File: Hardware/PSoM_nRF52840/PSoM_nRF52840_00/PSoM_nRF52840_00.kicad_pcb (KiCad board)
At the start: 6 copper layers, 26.3 x 23.2 mm, 52 parts, among them J1 Bare PCB USB C, J101 DF40C-60DP-0.4V(51), J401 Conn_01x01_Pin, J402 Conn_01x01_Pin, SW461 SW_Push, U201 NPM1300-QEAA-R, U401 nRF52840-QIAA-aQFN73, Y401 830108161301

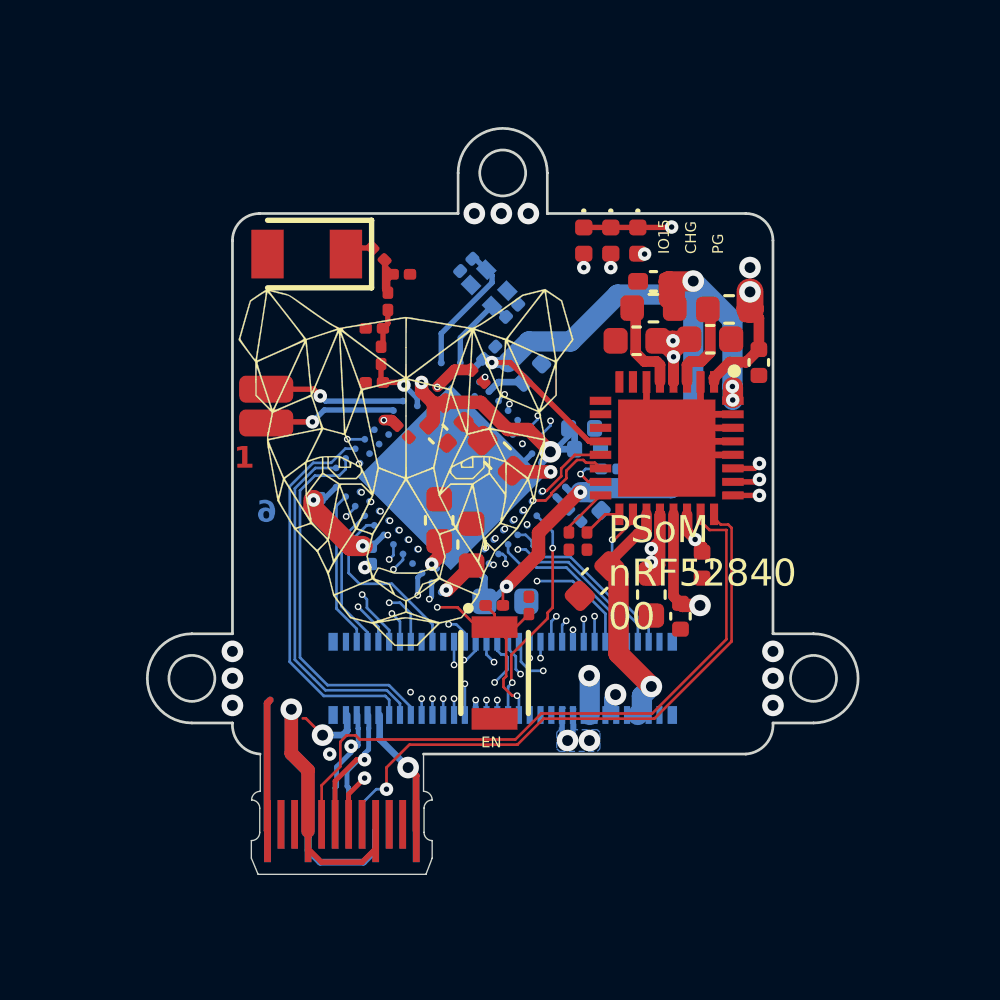
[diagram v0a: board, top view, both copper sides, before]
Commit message: rf routing to do
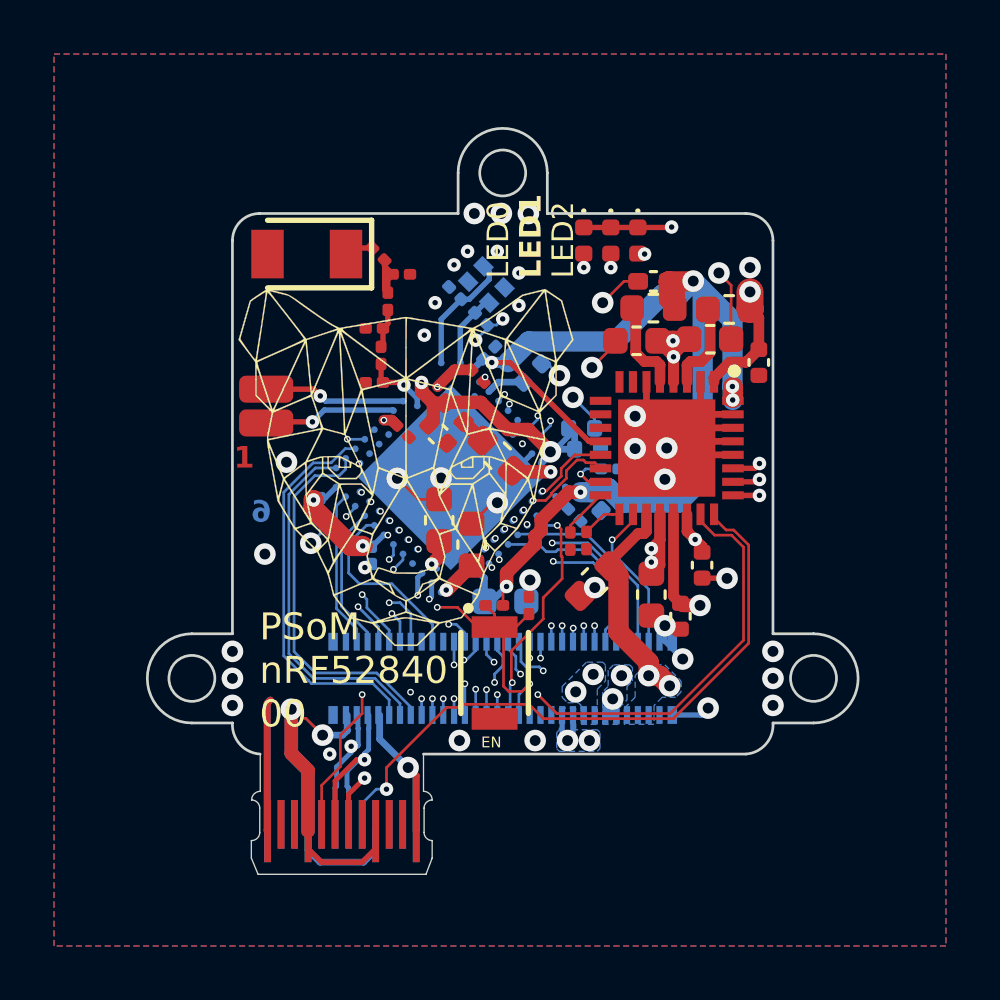
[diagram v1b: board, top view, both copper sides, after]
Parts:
- moved C402 1.19 mm to (135.2, 92.9), turned to -45 degrees
- moved C401 1.12 mm to (134.2, 91.9), turned to 135 degrees
- moved Y401 0.16 mm to (135.4, 91.6)
- moved R204 0.05 mm to (138.5, 101.1)
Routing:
- net GND: track 38.2 -> 64.4 mm, vias 12 -> 44
- net /100_Connectors/CC1: track 24.7 -> 27.0 mm, vias 0 -> 2
- net /200_1S_Charger/3V3_nRF: track 58.9 -> 60.3 mm
- net /100_Connectors/CC2: track 25.5 -> 26.9 mm
- net P11: track 6.37 -> 7.40 mm
- net /100_Connectors/RST: track 17.2 -> 18.2 mm
- net /200_1S_Charger/VBUS_OUT: track 13.5 -> 14.5 mm
- net /100_Connectors/VBAT: track 8.98 -> 8.21 mm, vias 1 -> 2
- net P5: track 6.57 -> 7.32 mm
- net VBUS: track 42.4 -> 43.1 mm, vias 3 -> 4
- net P9: track 6.19 -> 6.92 mm
- net P31: track 17.6 -> 16.9 mm
- net P7: track 6.94 -> 7.62 mm
- net P21: track 5.86 -> 5.19 mm
- net /100_Connectors/VSYS: track 35.6 -> 35.0 mm, vias 6 -> 7
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- added copper zone on B.Cu, net /100_Connectors/VBAT
- added copper zone on B.Cu, net /100_Connectors/VSYS
- added copper zone on B.Cu, net GND
- added copper zone on F.Cu, net GND
- added copper zone on In2.Cu, net GND
- added copper zone on In3.Cu, net GND
- added copper zone on B.Cu, net VBUS
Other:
- board text added: "LED0"
- board text added: "LED1"
- board text added: "LED2"
- board text removed: "CHG"
- board text removed: "IO15"
- board text removed: "PG"

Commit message: still need to do rf
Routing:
- net /400-nRF52840/DEC4_6: track 11.5 -> 12.5 mm
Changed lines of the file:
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@@
 	)
 	(via
-		(at 133.1 93.5)
+		(at 133.1 93.3)
 		(size 0.5)
 		(drill 0.2)
@@
 	)
 	(segment
-		(start 132.998492 95.580295)
-		(end 133.435839 96.017642)
+		(start 133.867642 96.017642)
+		(end 133.898412 95.986872)
 		(width 0.5)
 		(layer "F.Cu")
@@
 	)
 	(segment
-		(start 133.867642 96.017642)
-		(end 133.898412 95.986872)
+		(start 133.435839 96.017642)
+		(end 133.867642 96.017642)
 		(width 0.5)
 		(layer "F.Cu")
@@
 	)
 	(segment
-		(start 133.435839 96.017642)
-		(end 133.867642 96.017642)
+		(start 133.2 94.815)
+		(end 133.049033 94.965967)
 		(width 0.5)
 		(layer "F.Cu")
@@
 	)
 	(segment
-		(start 132.998492 95.251508)
-		(end 132.998492 95.580295)
+		(start 136.94589 96.992767)
+		(end 137.765169 97.812046)
 		(width 0.5)
 		(layer "F.Cu")
@@
 	)
 	(segment
-		(start 136.94589 96.992767)
-		(end 137.765169 97.812046)
+		(start 133.049033 94.965967)
+		(end 133.049033 95.630836)
 		(width 0.5)
 		(layer "F.Cu")
@@
 		(net 75)
 	)
+	(segment
+		(start 133.049033 95.630836)
+		(end 133.435839 96.017642)
+		(width 0.5)
+		(layer "F.Cu")
+		(net 75)
+	)
 	(via
 		(at 137.765169 97.816847)
@@
 	)
 	(via
-		(at 132.998492 95.251508)
+		(at 133.2 94.815)
 		(size 0.5)
 		(drill 0.2)
@@
 	)
 	(segment
+		(start 133.017767 95.232968)
+		(end 133.017767 94.997233)
+		(width 0.5)
+		(layer "B.Cu")
+		(net 75)
+	)
+	(segment
 		(start 137.954621 97.72)
 		(end 137.437184 98.237437)
@@
 	)
 	(segment
+		(start 133.017767 94.997233)
+		(end 133.2 94.815)
+		(width 0.5)
+		(layer "B.Cu")
+		(net 75)
+	)
+	(segment
 		(start 134.43198 94.525861)
 		(end 134.43198 93.215472)
@@
 	)
 	(segment
-		(start 129 97.680761)
-		(end 132.280761 94.4)
+		(start 132.580761 94.1)
+		(end 134.403837 94.1)
 		(width 0.75)
 		(layer "In3.Cu")
@@
 	)
 	(segment
-		(start 129 99.6)
-		(end 129 97.680761)
+		(start 134.703837 94.4)
+		(end 135.595882 94.4)
+		(width 0.75)
+		(layer "In3.Cu")
+		(net 92)
+	)
+	(segment
+		(start 134.403837 94.1)
+		(end 134.703837 94.4)
+		(width 0.75)
+		(layer "In3.Cu")
+		(net 92)
+	)
+	(segment
+		(start 129 97.680761)
+		(end 132.580761 94.1)
 		(width 0.75)
 		(layer "In3.Cu")
@@
 	)
 	(segment
-		(start 132.280761 94.4)
-		(end 135.595882 94.4)
+		(start 129 99.6)
+		(end 129 97.680761)
 		(width 0.75)
 		(layer "In3.Cu")

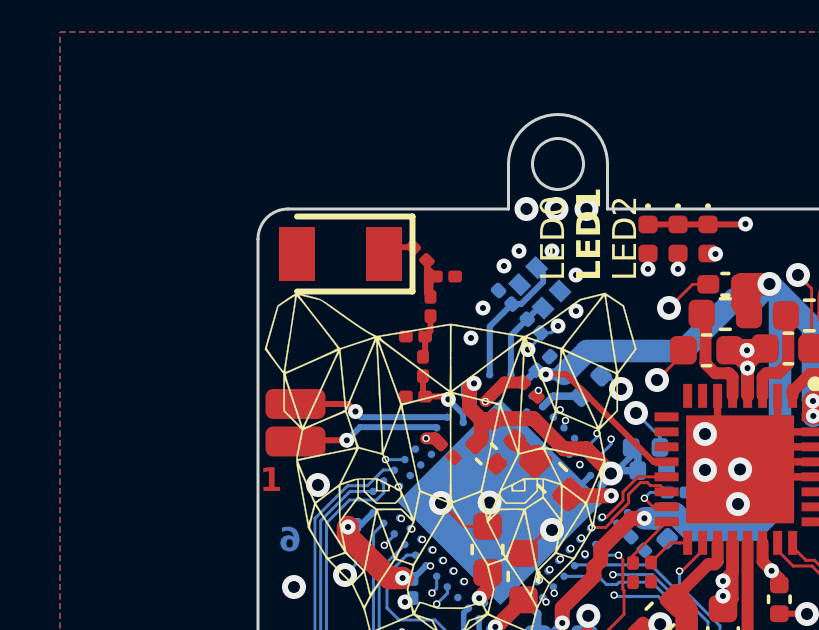
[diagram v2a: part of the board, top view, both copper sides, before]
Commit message: opened ground plane for antenna
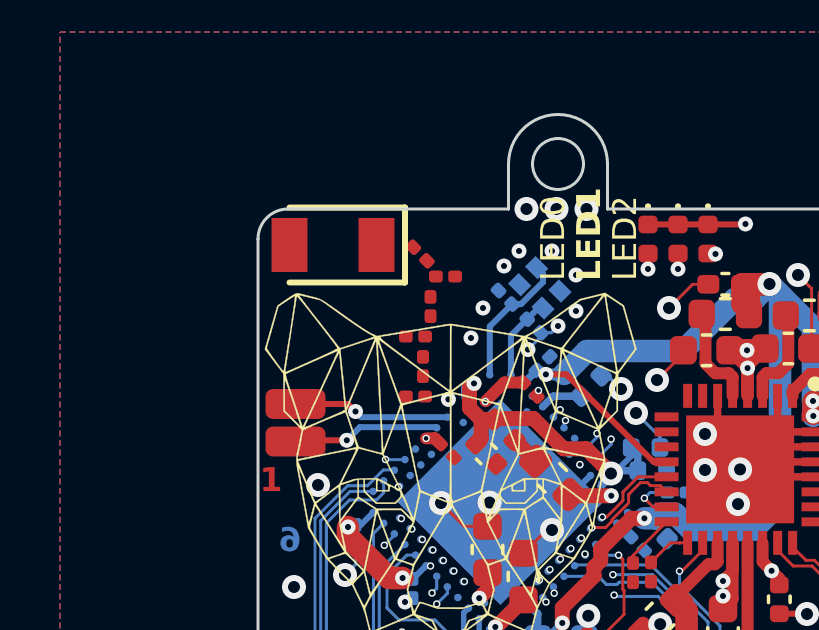
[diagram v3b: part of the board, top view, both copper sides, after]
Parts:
- moved ANT450 0.39 mm to (128.5, 90.2)
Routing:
- net /400-nRF52840/ANT_MATCH: track 2.65 -> 0.00 mm
- net /400-nRF52840/LNA_IN: track 2.50 -> 0.00 mm
- net /400-nRF52840/ANT_IN: track 1.46 -> 0.00 mm
- net /400-nRF52840/ANT_OUT: track 1.07 -> 0.00 mm
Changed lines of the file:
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@@
 	(footprint "Component_lib:ANTC3216X140N"
 		(layer "F.Cu")
-		(at 128.75 90.5 180)
+		(at 128.5 90.2 180)
 		(descr "2450AT18A100E")
 		(tags "Antenna")
@@
 		)
 	)
+	(dimension
+		(type aligned)
+		(layer "Dwgs.User")
+		(pts
+			(xy 126 89) (xy 133 89)
+		)
+		(height -2)
+		(gr_text "7.0000 mm"
+			(at 129.5 85.2 0)
+			(layer "Dwgs.User")
+			(effects
+				(font
+					(size 1.5 1.5)
+					(thickness 0.3)
+				)
+			)
+		)
+		(format
+			(prefix "")
+			(suffix "")
+			(units 3)
+			(units_format 1)
+			(precision 4)
+		)
+		(style
+			(thickness 0.2)
+			(arrow_length 1.27)
+			(text_position_mode 0)
+			(extension_height 0.58642)
+			(extension_offset 0.5) keep_text_aligned)
+	)
+	(dimension
+		(type aligned)
+		(layer "Dwgs.User")
+		(pts
+			(xy 126 89) (xy 126 95)
+		)
+		(height 4.999999)
+		(gr_text "6.0000 mm"
+			(at 119.200001 92 90)
+			(layer "Dwgs.User")
+			(effects
+				(font
+					(size 1.5 1.5)
+					(thickness 0.3)
+				)
+			)
+		)
+		(format
+			(prefix "")
+			(suffix "")
+			(units 3)
+			(units_format 1)
+			(precision 4)
+		)
+		(style
+			(thickness 0.2)
+			(arrow_length 1.27)
+			(text_position_mode 0)
+			(extension_height 0.58642)
+			(extension_offset 0.5) keep_text_aligned)
+	)
 	(segment
 		(start 142.069566 97.679527)
@@
 		(net 44)
 	)
-	(segment
-		(start 130.426274 90.273726)
-		(end 130.2 90.5)
-		(width 0.2)
-		(layer "F.Cu")
-		(net 45)
-	)
-	(segment
-		(start 131.178726 90.273726)
-		(end 130.426274 90.273726)
-		(width 0.2)
-		(layer "F.Cu")
-		(net 45)
-	)
-	(segment
-		(start 132.25 95.25)
-		(end 132.345962 95.345962)
-		(width 0.2)
-		(layer "F.Cu")
-		(net 46)
-	)
-	(segment
-		(start 131.5 94.57)
-		(end 131.5 95.18)
-		(width 0.2)
-		(layer "F.Cu")
-		(net 46)
-	)
-	(segment
-		(start 131.5 95.18)
-		(end 131.57 95.25)
-		(width 0.2)
-		(layer "F.Cu")
-		(net 46)
-	)
-	(segment
-		(start 131.57 95.25)
-		(end 132.25 95.25)
-		(width 0.2)
-		(layer "F.Cu")
-		(net 46)
-	)
 	(via
 		(at 132.345962 95.345962)
@@
 	)
 	(segment
-		(start 132.84099 95.84099)
-		(end 132.84099 96.116852)
-		(width 0.2)
-		(layer "B.Cu")
-		(net 46)
-	)
-	(segment
-		(start 132.345962 95.345962)
-		(end 132.84099 95.84099)
-		(width 0.2)
-		(layer "B.Cu")
-		(net 46)
-	)
-	(segment
-		(start 131.75 93.07)
-		(end 131.57 93.25)
-		(width 0.2)
-		(layer "F.Cu")
-		(net 47)
-	)
-	(segment
-		(start 131.75 92.57)
-		(end 131.75 93.07)
-		(width 0.2)
-		(layer "F.Cu")
-		(net 47)
-	)
-	(segment
-		(start 131.57 93.25)
-		(end 131.57 93.86)
-		(width 0.2)
-		(layer "F.Cu")
-		(net 47)
-	)
-	(segment
-		(start 131.57 93.86)
-		(end 131.5 93.93)
-		(width 0.2)
-		(layer "F.Cu")
-		(net 47)
-	)
-	(segment
-		(start 131.75 91.43)
-		(end 131.93 91.25)
-		(width 0.2)
-		(layer "F.Cu")
-		(net 48)
-	)
-	(segment
-		(start 131.631274 90.726274)
-		(end 131.631274 91.811274)
-		(width 0.2)
-		(layer "F.Cu")
-		(net 48)
-	)
-	(segment
-		(start 131.631274 90.726274)
-		(end 131.631274 90.951274)
-		(width 0.2)
-		(layer "F.Cu")
-		(net 48)
-	)
-	(segment
-		(start 131.631274 91.811274)
-		(end 131.75 91.93)
-		(width 0.2)
-		(layer "F.Cu")
-		(net 48)
-	)
-	(segment
-		(start 131.75 91.93)
-		(end 131.75 91.43)
-		(width 0.2)
-		(layer "F.Cu")
-		(net 48)
-	)
-	(segment
-		(start 131.631274 90.951274)
-		(end 131.93 91.25)
-		(width 0.2)
-		(layer "F.Cu")
-		(net 48)
-	)
-	(segment
 		(start 128.959799 96.709799)
 		(end 127.290201 96.709799)
@@
 		(polygon
 			(pts
-				(xy 126.25 89.1) (xy 131.95 89.1) (xy 131.95 92) (xy 126.25 92)
+				(xy 125.25 88.1) (xy 132.55 88.1) (xy 132.55 94.1) (xy 125.25 94.1)
 			)
 		)

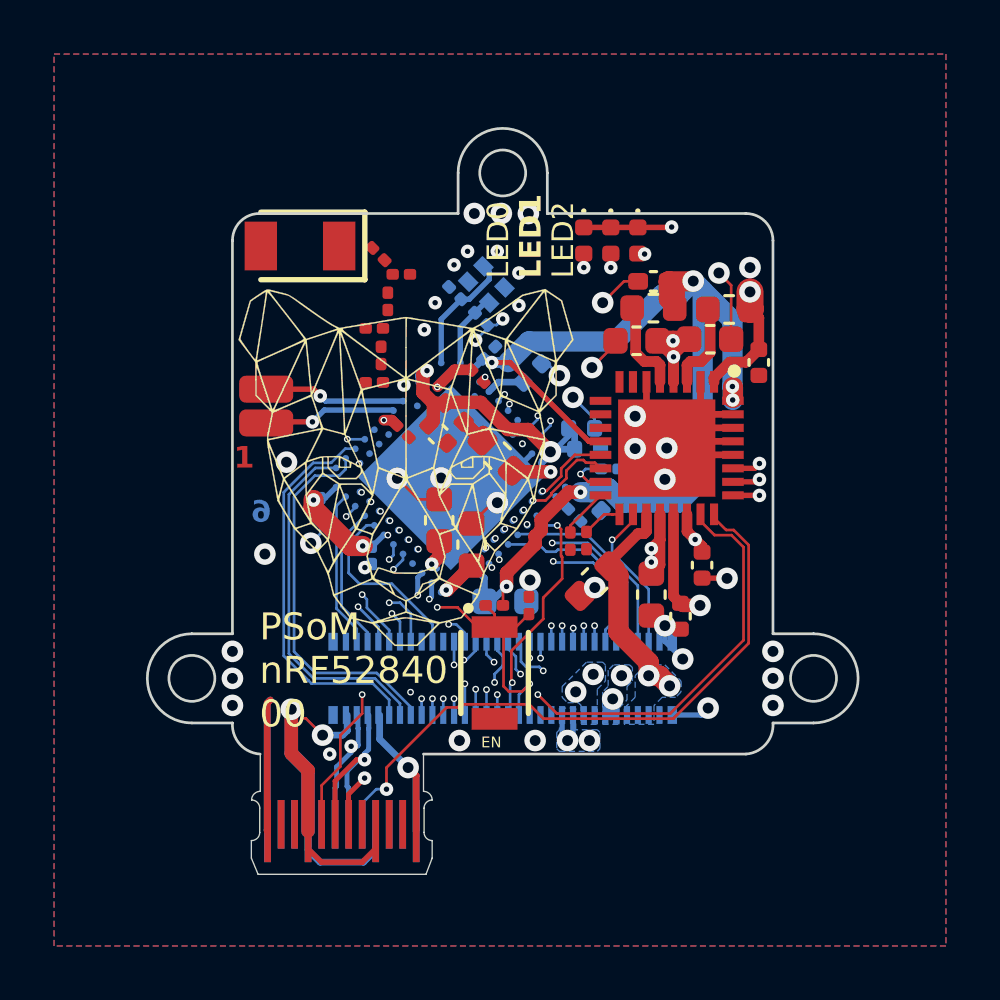
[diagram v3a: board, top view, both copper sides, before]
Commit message: added ufl connector and trace width for 50ohm rf
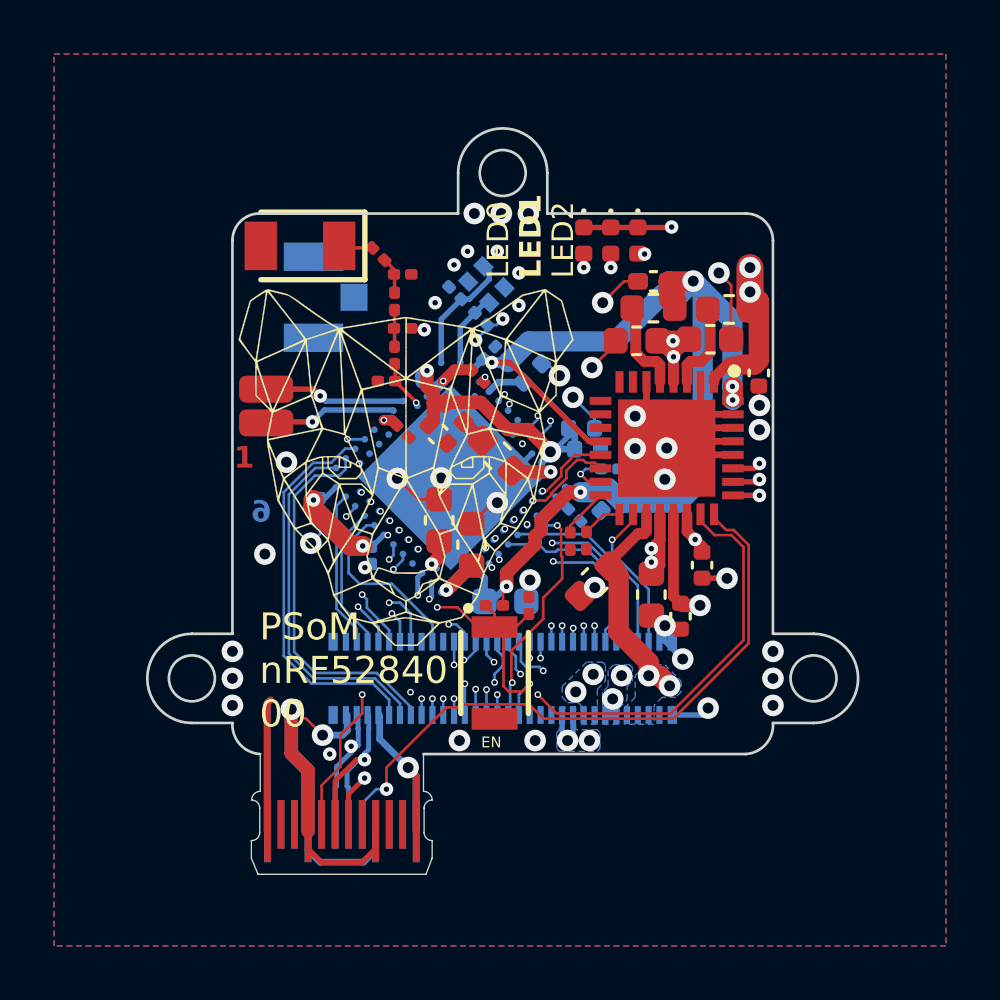
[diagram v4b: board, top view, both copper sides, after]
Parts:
- added J2: U.FL-R-SMT-1_40_, Component_lib:u.fl, B.Cu at (129.0, 92.1)
- moved C404 1.05 mm to (132.3, 93.2), turned to 0 degrees
- moved L401 0.50 mm to (132.0, 94.2)
- moved C403 0.45 mm to (131.7, 95.2)
- moved C207 0.39 mm to (145.5, 94.9)
- moved C451 0.25 mm to (132.0, 92.2)
- moved L452 0.05 mm to (132.3, 91.2)
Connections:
- net /400-nRF52840/LNA_IN renamed /400-nRF52840/ANT_LNA_IN
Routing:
- net +3V3: track 30.9 -> 35.2 mm
- net /400-nRF52840/ANT_LNA_IN: track 0.00 -> 1.90 mm
- net /400-nRF52840/ANT_IN: track 0.00 -> 1.36 mm
- net /400-nRF52840/ANT_MATCH: track 0.00 -> 1.36 mm
- net /400-nRF52840/ANT_OUT: track 0.00 -> 1.26 mm
- net GND: track 64.4 -> 65.1 mm, vias 44 -> 46

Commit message: finished routing + generated gerbers
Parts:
- removed ANT450: 2450AT18A100E, Component_lib:ANTC3216X140N
- removed C451: 1p, Capacitor_SMD:C_0201_0603Metric
- removed G***: LOGO, Component_lib:puma_logo_14mm
- removed L451: 3n9, Inductor_SMD:L_0201_0603Metric
- removed L452: 2n7, Inductor_SMD:L_0201_0603Metric
- J2: moved to F.Cu
- moved C404 1.78 mm to (130.8, 94.2), turned to -135 degrees
- moved C411 0.80 mm to (134.4, 94.5), turned to 135 degrees
- moved J2 0.66 mm to (128.7, 91.5), turned to 45 degrees
- moved C403 0.47 mm to (132.1, 95.4), turned to -135 degrees
- moved L401 0.46 mm to (131.7, 94.6), turned to -45 degrees
- moved D201 0.30 mm to (139.0, 90.3)
- moved D202 0.30 mm to (140.0, 90.3)
- moved D203 0.30 mm to (141.0, 90.3)
- moved C208 0.09 mm to (141.6, 91.6)
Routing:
- net GND: track 65.1 -> 76.6 mm, vias 46 -> 48
- net /100_Connectors/CC2: track 26.9 -> 24.0 mm, vias 2 -> 1
- net /400-nRF52840/ANT_MATCH: track 1.36 -> 0.00 mm
- net /400-nRF52840/ANT_OUT: track 1.26 -> 0.00 mm
- net /200_1S_Charger/3V3_nRF: track 60.6 -> 59.4 mm, vias 9 -> 8
- net /400-nRF52840/ANT_IN: track 1.36 -> 2.54 mm
- net P27: track 15.6 -> 14.7 mm
- net P25: track 13.0 -> 12.4 mm
- net P37: track 4.54 -> 3.96 mm
- net /100_Connectors/BATTERY_TEMP: track 5.64 -> 5.05 mm
- net /200_1S_Charger/VBUS_OUT: track 14.5 -> 13.9 mm
- added copper zone on F.Cu, net +3V3
- added copper zone on F.Cu, net /200_1S_Charger/3V3_nRF
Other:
- outline, holes or cut-outs redrawn
- board text added: "RST"
- board text removed: "EN"

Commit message: did some optimization on nrf52840_00
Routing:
- net /400-nRF52840/DEC4_6: track 12.4 -> 7.83 mm
- net GND: track 76.6 -> 75.6 mm
- net P34: track 8.19 -> 7.52 mm
- added copper zone on B.Cu, net /400-nRF52840/DEC4_6
